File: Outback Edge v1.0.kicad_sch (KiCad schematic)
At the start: 19 parts, among them J1 USB_C_Receptacle_USB2.0_16P, J2 OE_M.2_Socket_E, J3 RJ45_LED_Shielded, J4 Micro_SD_Card_Det_Hirose_DM3AT, J5 USB3_A_Stacked, SW1 SW_Push, U1 R7FA6M5AH3CFB#AA0, U2 USB2514B_Bi

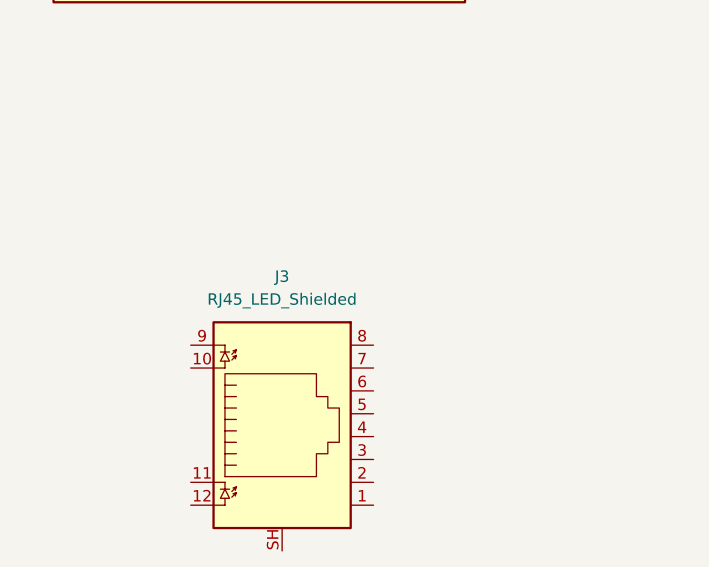
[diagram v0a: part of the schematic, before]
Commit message: Tie RJ45 shield to chassis
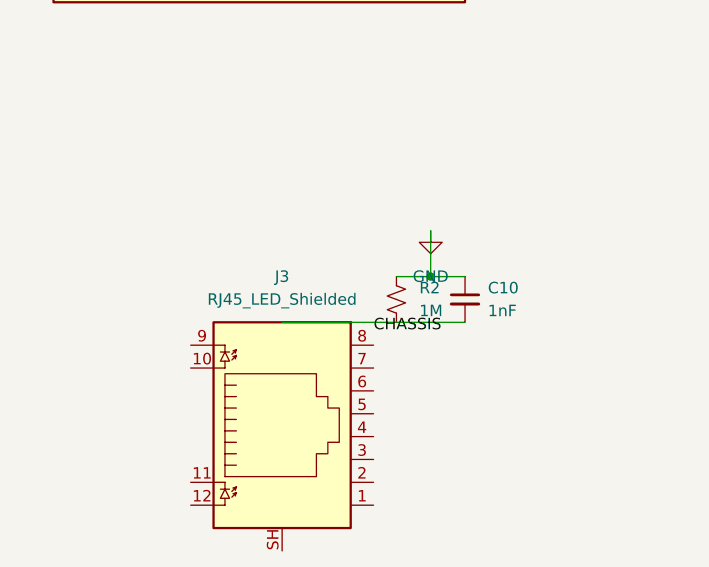
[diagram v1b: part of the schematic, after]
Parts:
- added C10: 1nF, Capacitor_SMD:C_0402_1005Metric, symbol Device:C_Small
- added R2: 1M, Resistor_SMD:R_0402_1005Metric, symbol Device:R_Small_US
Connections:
- net GND: now also C10.1, R2.1
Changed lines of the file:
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@@
 	)
 	(junction
+		(at 374.65 153.67)
+		(diameter 0)
+		(color 0 0 0 0)
+	)
+	(junction
 		(at 88.9 157.48)
 		(diameter 0)
@@
 	(wire
 		(pts
+			(xy 358.14 158.75) (xy 378.46 158.75)
+		)
+		(stroke
+			(width 0)
+			(type default)
+		)
+	)
+	(wire
+		(pts
+			(xy 370.84 153.67) (xy 378.46 153.67)
+		)
+		(stroke
+			(width 0)
+			(type default)
+		)
+	)
+	(wire
+		(pts
+			(xy 374.65 153.67) (xy 374.65 148.59)
+		)
+		(stroke
+			(width 0)
+			(type default)
+		)
+	)
+	(wire
+		(pts
 			(xy 113.03 271.78) (xy 113.03 261.62)
 		)
@@
 		)
 	)
+	(label "CHASSIS"
+		(at 368.3 160.02 0)
+		(effects
+			(font
+				(size 1.27 1.27)
+			)
+			(justify left bottom)
+		)
+	)
 	(label "SDIO_CLK"
 		(at 115.57 271.78 90)
@@
 					(unit 1)
 				)
+			)
+		)
+	)
+	(symbol
+		(lib_id "Device:R_Small_US")
+		(at 370.84 156.21 0)
+		(unit 1)
+		(exclude_from_sim no)
+		(in_bom yes)
+		(on_board yes)
+		(dnp no)
+		(property "Reference" "R2"
+			(at 373.38 154.94 0)
+			(effects
+				(font
+					(size 1.27 1.27)
+				)
+				(justify left)
+			)
+		)
+		(property "Value" "1M"
+			(at 373.38 157.48 0)
+			(effects
+				(font
+					(size 1.27 1.27)
+				)
+				(justify left)
+			)
+		)
+		(property "Footprint" "Resistor_SMD:R_0402_1005Metric"
+			(at 370.84 156.21 0)
+			(effects
+				(font
+					(size 1.27 1.27)
+				)
+				(hide yes)
+			)
+		)
+		(property "Datasheet" "~"
+			(at 370.84 156.21 0)
+			(effects
+				(font
+					(size 1.27 1.27)
+				)
+				(hide yes)
+			)
+		)
+		(property "Description" "Resistor, small US symbol"
+			(at 370.84 156.21 0)
+			(effects
+				(font
+					(size 1.27 1.27)
+				)
+				(hide yes)
+			)
+		)
+		(pin "1"
+		)
+		(pin "2"
+		)
+		(instances
+			(project ""
+				(path "/d62ee704-355f-444e-be1b-61eabb2fe2aa"
+					(reference "R2")
+					(unit 1)
+				)
+			)
+		)
+	)
+	(symbol
+		(lib_id "Device:C_Small")
+		(at 378.46 156.21 0)
+		(unit 1)
+		(exclude_from_sim no)
+		(in_bom yes)
+		(on_board yes)
+		(dnp no)
+		(property "Reference" "C10"
+			(at 381 154.94 0)
+			(effects
+				(font
+					(size 1.27 1.27)
+				)
+				(justify left)
+			)
+		)
+		(property "Value" "1nF"
+			(at 381 157.48 0)
+			(effects
+				(font
+					(size 1.27 1.27)
+				)
+				(justify left)
+			)
+		)
+		(property "Footprint" "Capacitor_SMD:C_0402_1005Metric"
+			(at 378.46 156.21 0)
+			(effects
+				(font
+					(size 1.27 1.27)
+				)
+				(hide yes)
+			)
+		)
+		(property "Datasheet" "~"
+			(at 378.46 156.21 0)
+			(effects
+				(font
+					(size 1.27 1.27)
+				)
+				(hide yes)
+			)
+		)
+		(property "Description" "Unpolarized capacitor, small symbol"
+			(at 378.46 156.21 0)
+			(effects
+				(font
+					(size 1.27 1.27)
+				)
+				(hide yes)
+			)
+		)
+		(pin "2"
+		)
+		(pin "1"
+		)
+		(instances
+			(project "Outback Edge v1.0"
+				(path "/d62ee704-355f-444e-be1b-61eabb2fe2aa"
+					(reference "C10")
+					(unit 1)
+				)
+			)
+		)
+	)
+	(symbol
+		(lib_id "power:GND")
+		(at 374.65 148.59 0)
+		(unit 1)
+		(exclude_from_sim no)
+		(in_bom yes)
+		(on_board yes)
+		(dnp no)
+		(fields_autoplaced yes)
+		(property "Reference" "#PWR042"
+			(at 374.65 154.94 0)
+			(effects
+				(font
+					(size 1.27 1.27)
+				)
+				(hide yes)
+			)
+		)
+		(property "Value" "GND"
+			(at 374.65 153.67 0)
+			(effects
+				(font
+					(size 1.27 1.27)
+				)
+			)
+		)
+		(property "Footprint" ""
+			(at 374.65 148.59 0)
+			(effects
+				(font
+					(size 1.27 1.27)
+				)
+				(hide yes)
+			)
+		)
+		(property "Datasheet" ""
+			(at 374.65 148.59 0)
+			(effects
+				(font
+					(size 1.27 1.27)
+				)
+				(hide yes)
+			)
+		)
+		(property "Description" "Power symbol creates a global label with name \"GND\" , ground"
+			(at 374.65 148.59 0)
+			(effects
+				(font
+					(size 1.27 1.27)
+				)
+				(hide yes)
+			)
+		)
+		(pin "1"
+		)
+		(instances
+			(project "Outback Edge v1.0"
+				(path "/d62ee704-355f-444e-be1b-61eabb2fe2aa"
+					(reference "#PWR042")
+					(unit 1)
+				)
